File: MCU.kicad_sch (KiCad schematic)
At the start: 29 parts, among them J3 Conn_01x02_Socket, J4 Conn_01x02_Socket, U3 TPS56A37RPAR, U4 ATSAMD21G18A-A

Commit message: Added USB C, LDO regulator and sections off schematic in pages to make readable
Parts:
- removed BT2: 5V (Battery_Cell), symbol Device:Battery_Cell
- removed C19, C20: 10u, symbol Device:C_Polarized
- removed C21, C24: 100n, symbol Device:C_Polarized
- removed C22: 22n, symbol Device:C
- removed C23: 100n, symbol Device:C
- removed C25: 30p, symbol Device:C_Polarized
- removed C26: 215.061, symbol Device:C_Polarized
- removed J3, J4: Conn_01x02_Socket, symbol Connector:Conn_01x02_Socket
- removed L2: 6.8u, symbol Device:L
- removed R10: 20k, symbol Device:R
- removed R6: 52k3, symbol Device:R
- removed R7: 250R, symbol Device:R
- removed R8: 100k, symbol Device:R
- removed R9: 412k, symbol Device:R
- removed U3: TPS56A37RPAR, RPA0010A-MFG, symbol Imported_ICs:TPS56A37RPAR
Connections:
- net USB_D-: now reaches U4.33 (PA24)
- net USB_D+: now reaches U4.34 (PA25)
- no-connect marks 1 -> 0
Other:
- moved on the sheet: C27, C28, C29, C30, C31, C32, C33, C34, C35, C36, U4

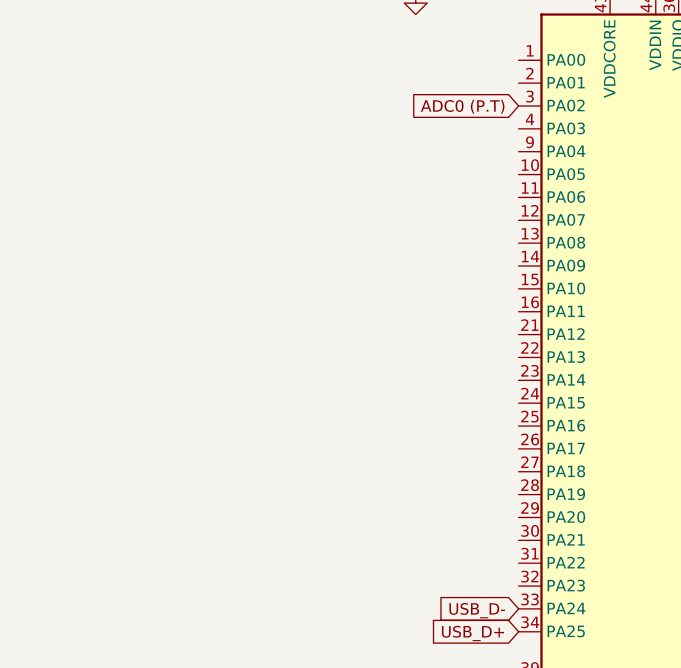
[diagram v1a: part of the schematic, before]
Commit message: Changes before syncing to main. Adding crystal as well as Thermocouple sensor and buck 3.3V step down
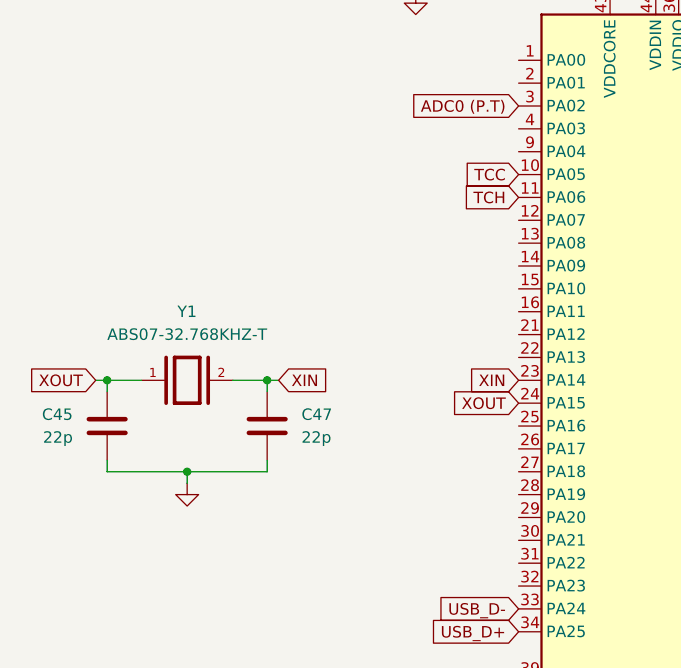
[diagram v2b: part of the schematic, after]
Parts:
- added C45, C47: 22p, symbol Device:C
- added Y1: ABS07-32.768KHZ-T, ABS07-32.768KHZ-T:XTAL_ABS07-32.768KHZ-T, symbol Imported_ICs:ABS07-32.768KHZ-T
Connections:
- net GND: now also C45.2, C47.2
- net TCC: now reaches U4.10 (PA05)
- net TCH: now reaches U4.11 (PA06)
- net XIN: now reaches U4.23 (PA14)
- net XIN: now also C47.1, Y1.2
- net XOUT: now reaches U4.24 (PA15)
- net XOUT: now also C45.1, Y1.1

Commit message: Added changes to pass ERC check
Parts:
- added C25: 100n, symbol Device:C
- added R45: 10k, symbol Device:R
- added R46: 330R, symbol Device:R
- added SW1: SW_Push, Button_Switch_SMD:SW_SPST_B3S-1000, symbol Switch:SW_Push
- renumbered C45 to C13, C47 to C14, C27 to C15, C28 to C16, C29 to C17, C30 to C18, C31 to C19, C32 to C20, C33 to C21, C34 to C22, C35 to C23, C36 to C24, U4 to U6
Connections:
- net +3.3V: now also R45.1
- net GND: now also C25.2, SW1.1
- net Valve1: now reaches U6.25 (PA16)
- net Valve2: now reaches U6.26 (PA17)
- net Valve3: now reaches U6.27 (PA18)
- net Valve4: now reaches U6.28 (PA19)
- net Valve5: now reaches U6.29 (PA20)
- net Valve6: now reaches U6.30 (PA21)
- net at U6.40 (~{RESET}): now also C25.1, R45.2, R46.2
- new net: R46.1, SW1.2
- no-connect marks 0 -> 25
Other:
- moved on the sheet: C13, C14, Y1

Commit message: added footprints to every component except inductors. That will be in the next commit
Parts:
- C13, C14, C15, C16, C17, C18, C19, C20, C21, C22, C23, C24, C25: footprint (none) -> Capacitor_SMD:C_0402_1005Metric
- R45, R46: footprint (none) -> Resistor_SMD:R_0402_1005Metric
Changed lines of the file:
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@@
 			)
 		)
-		(property "Footprint" ""
+		(property "Footprint" "Capacitor_SMD:C_0402_1005Metric"
 			(at 174.9552 41.91 0)
 			(hide yes)
@@
 			)
 		)
-		(property "Footprint" ""
+		(property "Footprint" "Resistor_SMD:R_0402_1005Metric"
 			(at 100.33 155.448 90)
 			(hide yes)
@@
 			)
 		)
-		(property "Footprint" ""
+		(property "Footprint" "Capacitor_SMD:C_0402_1005Metric"
 			(at 150.8252 41.91 0)
 			(hide yes)
@@
 			)
 		)
-		(property "Footprint" ""
+		(property "Footprint" "Capacitor_SMD:C_0402_1005Metric"
 			(at 127.3048 41.91 0)
 			(hide yes)
@@
 			)
 		)
-		(property "Footprint" ""
+		(property "Footprint" "Capacitor_SMD:C_0402_1005Metric"
 			(at 111.4552 59.69 0)
 			(hide yes)
@@
 			)
 		)
-		(property "Footprint" ""
+		(property "Footprint" "Capacitor_SMD:C_0402_1005Metric"
 			(at 157.1752 58.42 0)
 			(hide yes)
@@
 			)
 		)
-		(property "Footprint" ""
+		(property "Footprint" "Resistor_SMD:R_0402_1005Metric"
 			(at 106.172 148.59 90)
 			(hide yes)
@@
 			)
 		)
-		(property "Footprint" ""
+		(property "Footprint" "Capacitor_SMD:C_0402_1005Metric"
 			(at 68.8848 87.63 0)
 			(hide yes)
@@
 			)
 		)
-		(property "Footprint" ""
+		(property "Footprint" "Capacitor_SMD:C_0402_1005Metric"
 			(at 169.8752 58.42 0)
 			(hide yes)
@@
 			)
 		)
-		(property "Footprint" ""
+		(property "Footprint" "Capacitor_SMD:C_0402_1005Metric"
 			(at 121.6152 59.69 0)
 			(hide yes)
@@
 			)
 		)
-		(property "Footprint" ""
+		(property "Footprint" "Capacitor_SMD:C_0402_1005Metric"
 			(at 88.5952 87.63 0)
 			(hide yes)
@@
 			)
 		)
-		(property "Footprint" ""
+		(property "Footprint" "Capacitor_SMD:C_0402_1005Metric"
 			(at 181.3052 58.42 0)
 			(hide yes)
@@
 			)
 		)
-		(property "Footprint" ""
+		(property "Footprint" "Capacitor_SMD:C_0402_1005Metric"
 			(at 162.2552 41.91 0)
 			(hide yes)
@@
 			)
 		)
-		(property "Footprint" ""
+		(property "Footprint" "Capacitor_SMD:C_0402_1005Metric"
 			(at 116.5352 163.83 0)
 			(hide yes)
@@
 			)
 		)
-		(property "Footprint" ""
+		(property "Footprint" "Capacitor_SMD:C_0402_1005Metric"
 			(at 114.6048 41.91 0)
 			(hide yes)

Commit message: Added final missing footprints, ready to set drc
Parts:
- Y1: footprint ABS07-32.768KHZ-T:XTAL_ABS07-32.768KHZ-T -> Library:XTAL_ABS07-32.768KHZ-T
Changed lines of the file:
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@@
 			)
 		)
-		(property "Footprint" "ABS07-32.768KHZ-T:XTAL_ABS07-32.768KHZ-T"
+		(property "Footprint" "Library:XTAL_ABS07-32.768KHZ-T"
 			(at 78.74 78.74 0)
 			(hide yes)
